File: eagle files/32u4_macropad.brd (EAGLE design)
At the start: 75.2 x 98.6 mm, 91 parts, among them J1 TYPE-C-31-M-12, Q1 16MHz, SW2 SWITCH-SMD-EVP-BB2A9B00

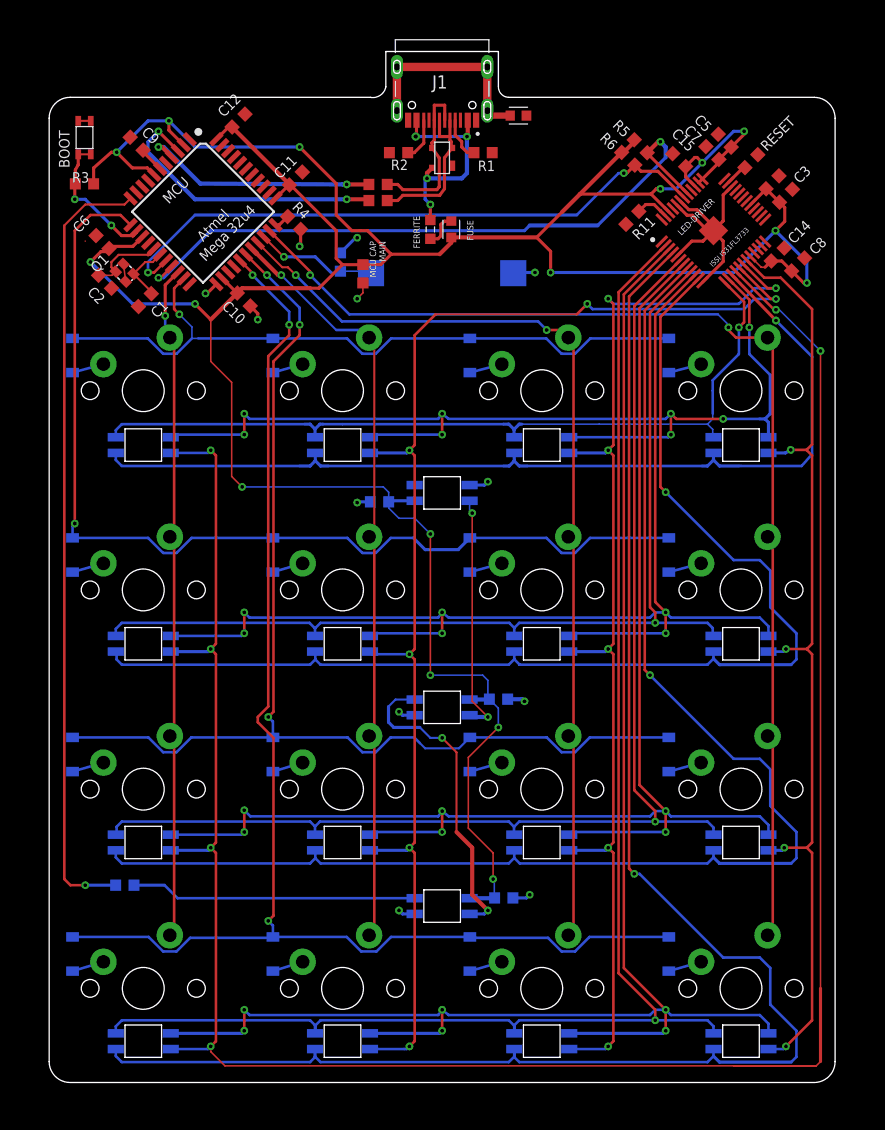
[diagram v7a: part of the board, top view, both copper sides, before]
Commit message: Added rendering folder, enlargerd gnd plane, traces width corrected
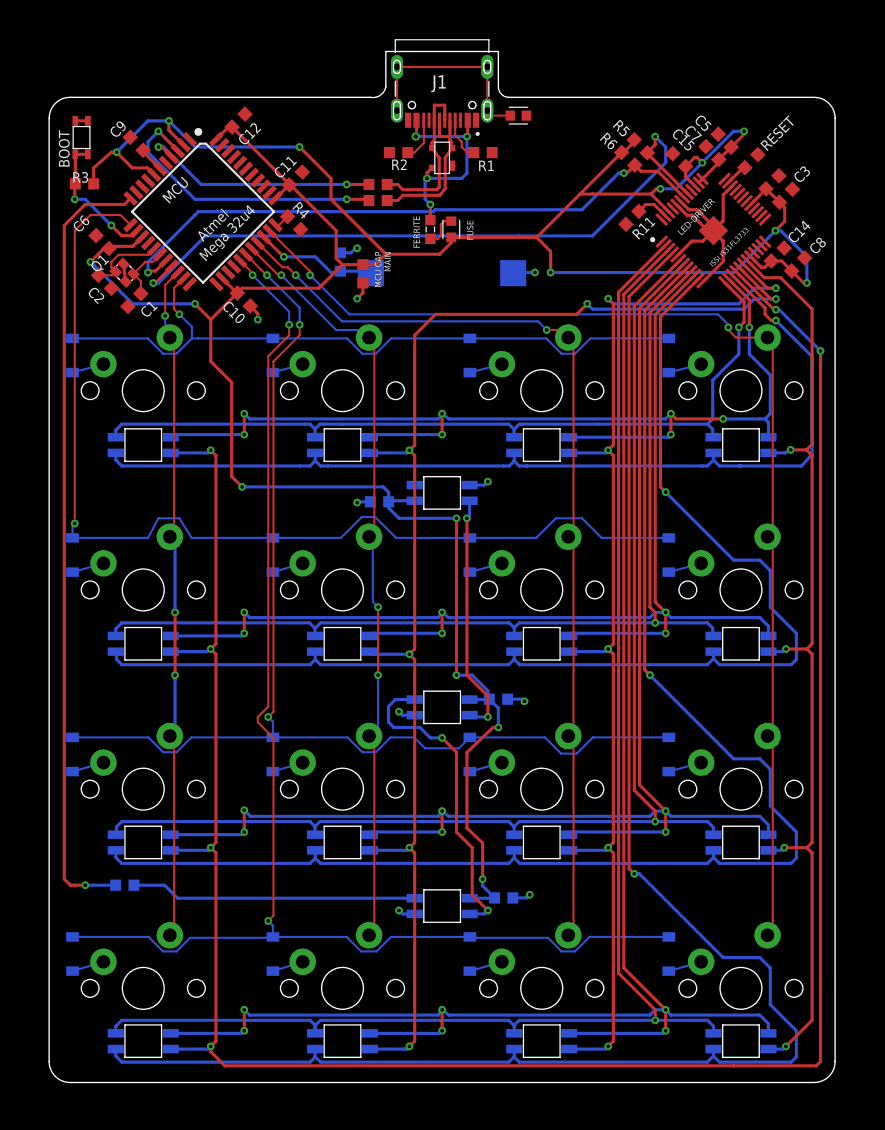
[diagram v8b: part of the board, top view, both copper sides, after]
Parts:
- moved C1 1.00 mm to (18.2, 84.9)
- moved SW2 0.28 mm to (13.2, 100.4)
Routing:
- net GND: track 49.3 -> 45.9 mm, vias 12 -> 10
- net SDA: track 64.1 -> 66.7 mm
- net VCC: track 305.6 -> 304.6 mm
- net R1SWTCH: track 97.3 -> 98.2 mm
- net C1SWTCH: track 73.1 -> 73.4 mm, vias 1 -> 3
- net C0SWTCH: track 65.1 -> 65.2 mm, vias 1 -> 3
